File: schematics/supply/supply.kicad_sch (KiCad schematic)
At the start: 4 parts, among them J1 Conn_01x02_Pin, J2 Conn_01x02_Pin, J3 Conn_01x01_Pin, J4 Conn_01x01_Pin

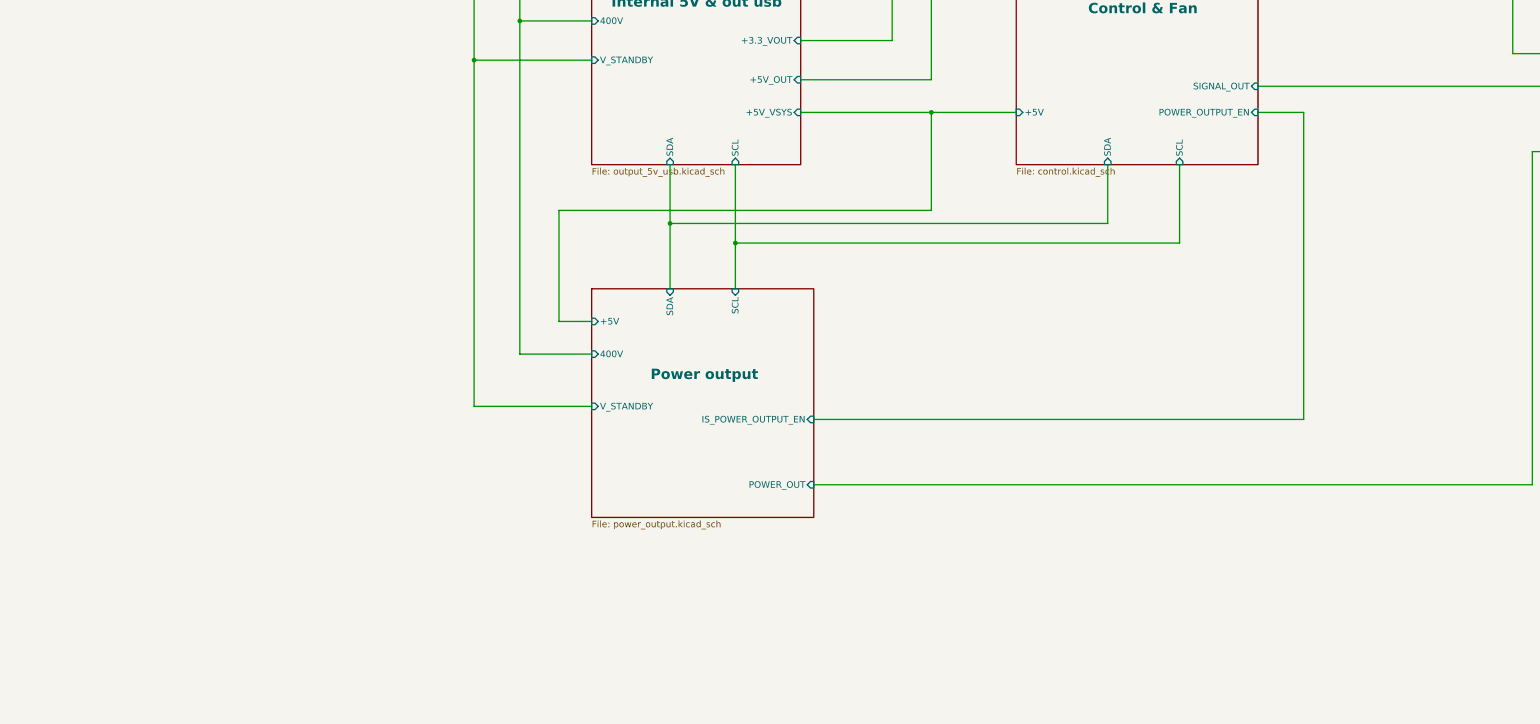
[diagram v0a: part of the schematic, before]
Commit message: Prepare to move USB ports to a few millimenters outside
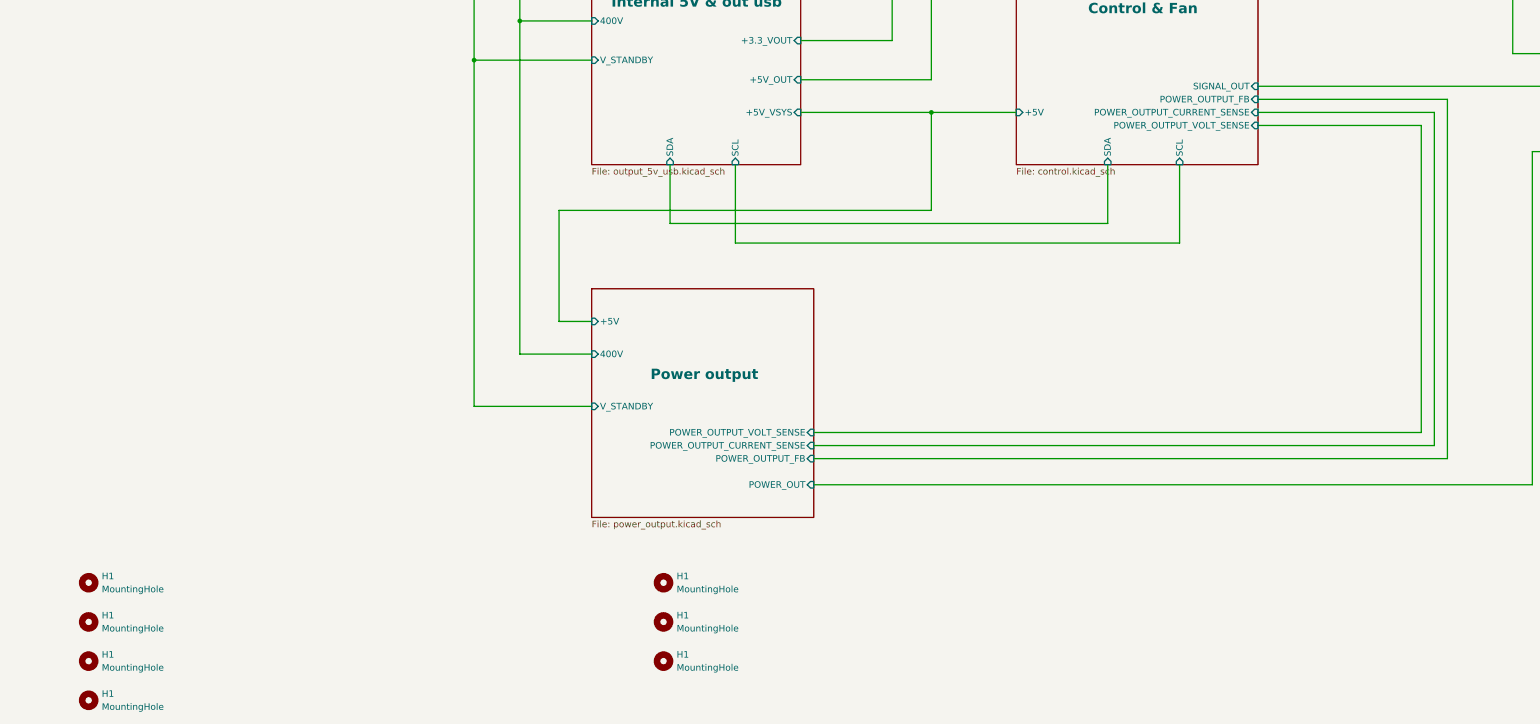
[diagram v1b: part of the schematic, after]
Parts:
- added H1 (x7): MountingHole, MountingHole:MountingHole_2.2mm_M2, symbol Mechanical:MountingHole
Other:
- sheet Control & Fan ports: added POWER_OUTPUT_CURRENT_SENSE, POWER_OUTPUT_FB, POWER_OUTPUT_VOLT_SENSE; removed POWER_OUTPUT_EN
- sheet Power output ports: added POWER_OUTPUT_CURRENT_SENSE, POWER_OUTPUT_FB, POWER_OUTPUT_VOLT_SENSE; removed IS_POWER_OUTPUT_EN, SCL, SDA

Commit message: Updated boards
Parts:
- added H1 (x2): MountingHole, MountingHole:MountingHole_2.2mm_M2, symbol Mechanical:MountingHole
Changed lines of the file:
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@@
+    )
+  )
+  (symbol (lib_id "Mechanical:MountingHole") (at 31.75 269.24 0) (unit 1)
+    (in_bom yes) (on_board yes) (dnp no) (fields_autoplaced)
+    (property "Reference" "H1" (at 34.29 267.9699 0)
+      (effects (font (size 1.27 1.27)) (justify left))
+    )
+    (property "Value" "MountingHole" (at 34.29 270.5099 0)
+      (effects (font (size 1.27 1.27)) (justify left))
+    )
+    (property "Footprint" "MountingHole:MountingHole_2.2mm_M2" (at 31.75 269.24 0)
+      (effects (font (size 1.27 1.27)) hide)
+    )
+    (property "Datasheet" "~" (at 31.75 269.24 0)
+      (effects (font (size 1.27 1.27)) hide)
+    )
+    (instances
+      (project "xray"
+        (path "/002cc585-3681-421a-8dca-b0910197d82b"
+          (reference "H1") (unit 1)
+        )
+      )
+      (project "supply"
+        (path "/1e139717-fcd1-4008-a6ea-4c993845e928"
+          (reference "H5") (unit 1)
+        )
+      )
+    )
+  )
+  (symbol (lib_id "Mechanical:MountingHole") (at 31.75 276.86 0) (unit 1)
+    (in_bom yes) (on_board yes) (dnp no) (fields_autoplaced)
+    (property "Reference" "H1" (at 34.29 275.5899 0)
+      (effects (font (size 1.27 1.27)) (justify left))
+    )
+    (property "Value" "MountingHole" (at 34.29 278.1299 0)
+      (effects (font (size 1.27 1.27)) (justify left))
+    )
+    (property "Footprint" "MountingHole:MountingHole_2.2mm_M2" (at 31.75 276.86 0)
+      (effects (font (size 1.27 1.27)) hide)
+    )
+    (property "Datasheet" "~" (at 31.75 276.86 0)
+      (effects (font (size 1.27 1.27)) hide)
+    )
+    (instances
+      (project "xray"
+        (path "/002cc585-3681-421a-8dca-b0910197d82b"
+          (reference "H1") (unit 1)
+        )
+      )
+      (project "supply"
+        (path "/1e139717-fcd1-4008-a6ea-4c993845e928"
+          (reference "H6") (unit 1)
+        )
+      )
     )
   )
@@
       (project "supply"
         (path "/1e139717-fcd1-4008-a6ea-4c993845e928"
-          (reference "H5") (unit 1)
+          (reference "H7") (unit 1)
         )
       )
@@
       (project "supply"
         (path "/1e139717-fcd1-4008-a6ea-4c993845e928"
-          (reference "H7") (unit 1)
+          (reference "H9") (unit 1)
         )
       )
@@
       (project "supply"
         (path "/1e139717-fcd1-4008-a6ea-4c993845e928"
-          (reference "H6") (unit 1)
-        )
-      )
+          (reference "H8") (unit 1)
+        )
+      )

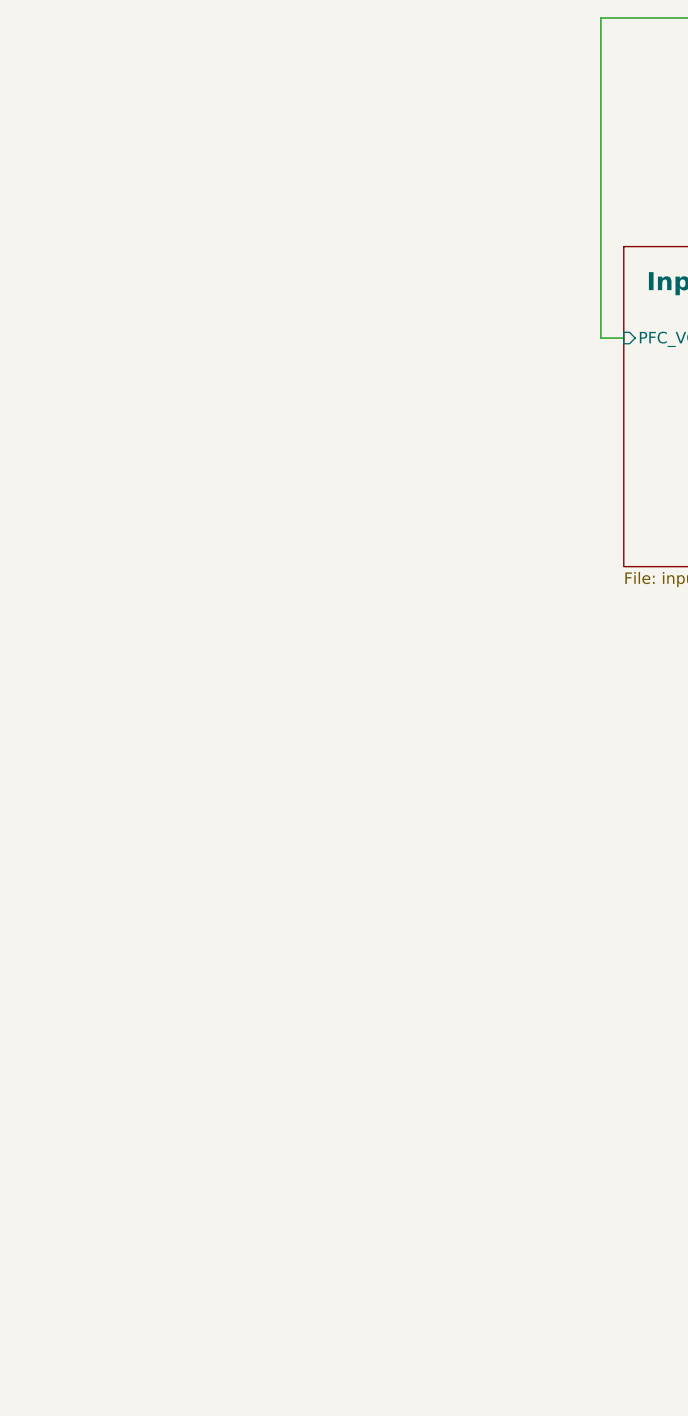
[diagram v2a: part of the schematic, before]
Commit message: prepare to add current measurement for a middle-current 5V and 3.3V lines
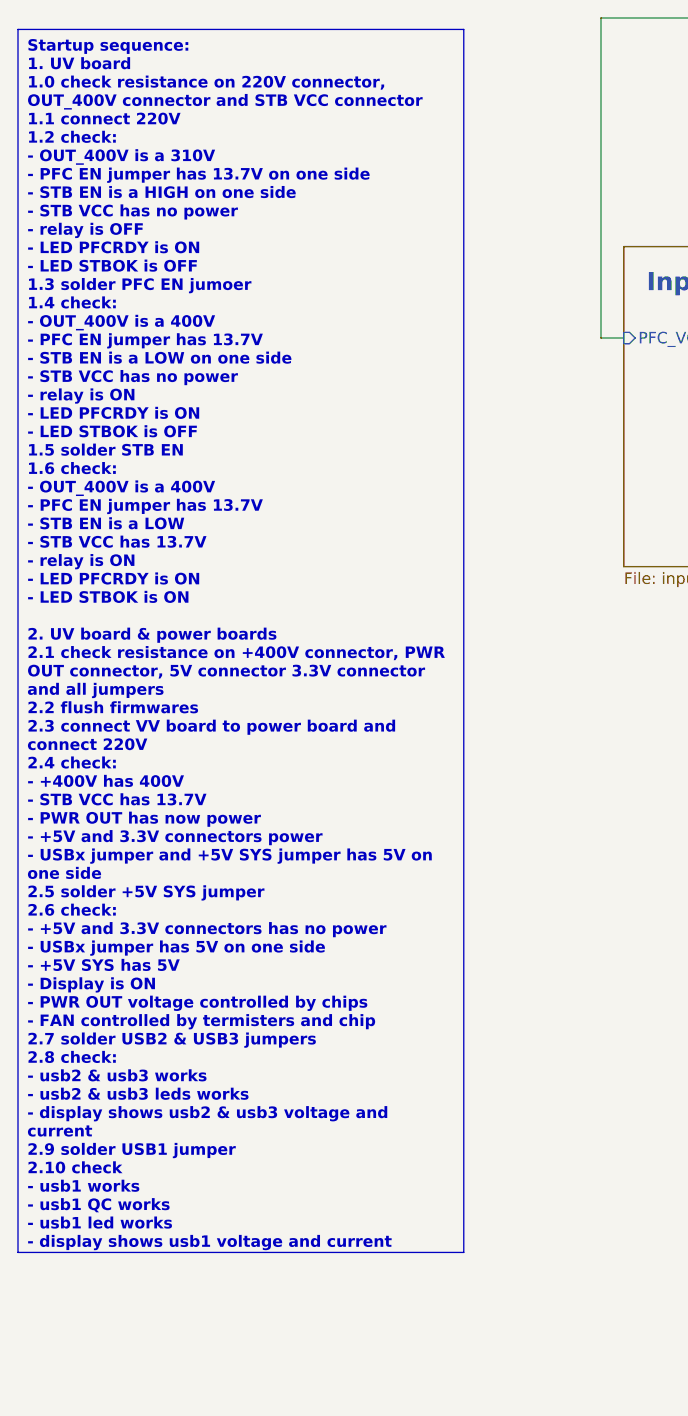
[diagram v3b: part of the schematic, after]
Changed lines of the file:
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@@
     (stroke (width 0) (type default))
+  )
+  (text_box "Startup sequence:\n1. UV board\n1.0 check resistance on 220V connector, OUT_400V connector and STB VCC connector\n1.1 connect 220V\n1.2 check: \n    - OUT_400V is a 310V\n    - PFC EN jumper has 13.7V on one side \n    - STB EN is a HIGH on one side\n    - STB VCC has no power\n    - relay is OFF\n    - LED PFCRDY is ON\n    - LED STBOK is OFF\n1.3 solder PFC EN jumoer\n1.4 check:\n    - OUT_400V is a 400V\n    - PFC EN jumper has 13.7V\n    - STB EN is a LOW on one side\n    - STB VCC has no power\n    - relay is ON\n    - LED PFCRDY is ON\n    - LED STBOK is OFF\n1.5 solder STB EN\n1.6 check:\n    - OUT_400V is a 400V\n    - PFC EN jumper has 13.7V\n    - STB EN is a LOW\n    - STB VCC has 13.7V\n    - relay is ON\n    - LED PFCRDY is ON\n    - LED STBOK is ON\n\n2. UV board & power boards\n2.1 check resistance on +400V connector, PWR OUT connector, 5V connector 3.3V connector and all jumpers\n2.2 flush firmwares\n2.3 connect VV board to power board and connect 220V\n2.4 check:\n    - +400V has 400V\n    - STB VCC has 13.7V\n    - PWR OUT has now power\n    - +5V and 3.3V connectors power\n    - USBx jumper and +5V SYS jumper has 5V on one side\n2.5 solder +5V SYS jumper\n2.6 check:\n    - +5V and 3.3V connectors has no power\n    - USBx jumper has 5V on one side\n    - +5V SYS has 5V\n    - Display is ON\n    - PWR OUT voltage controlled by chips\n    - FAN controlled by termisters and chip\n2.7 solder USB2 & USB3 jumpers\n2.8 check: \n    - usb2 & usb3 works\n    - usb2 & usb3 leds works\n    - display shows usb2 & usb3 voltage and current\n2.9 solder USB1 jumper\n2.10 check \n    - usb1 works\n    - usb1 QC works\n    - usb1 led works\n    - display shows usb1 voltage and current\n"
+    (at -48.26 30.48 0) (size 49.53 135.89)
+    (stroke (width 0) (type default))
+    (fill (type none))
+    (effects (font (size 1.27 1.27) (thickness 0.254) bold) (justify left top))
   )
   (symbol (lib_id "Mechanical:MountingHole") (at 31.75 254 0) (unit 1)

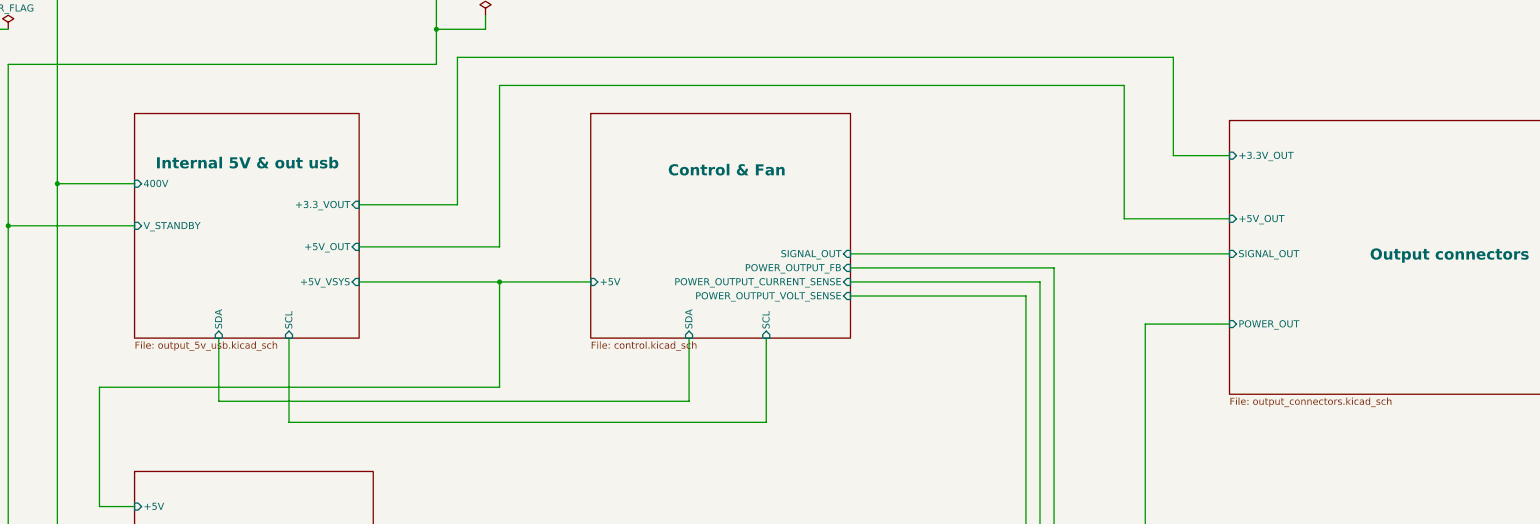
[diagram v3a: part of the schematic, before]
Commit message: prepare to replace inductor on 5V power line
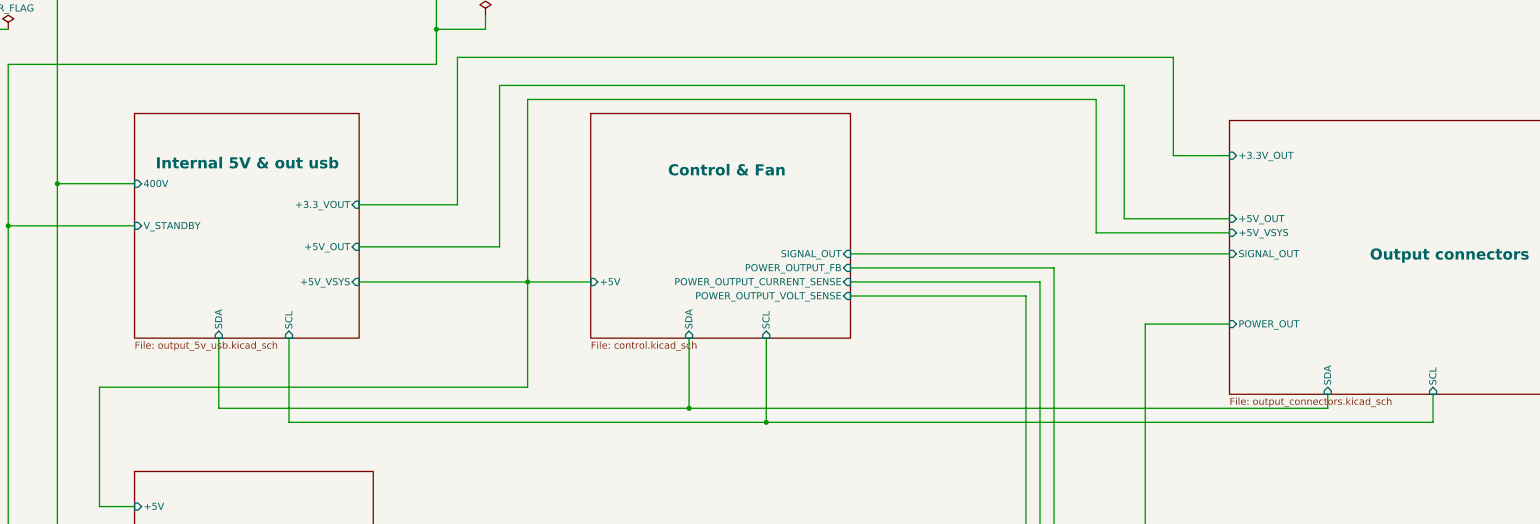
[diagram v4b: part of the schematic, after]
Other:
- sheet Output connectors ports: added +5V_VSYS, SCL, SDA; removed none
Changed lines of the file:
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@@
   (junction (at 184.15 101.6) (diameter 0) (color 0 0 0 0)
   )
-  (junction (at 195.58 147.32) (diameter 0) (color 0 0 0 0)
-  )
   (junction (at 97.79 101.6) (diameter 0) (color 0 0 0 0)
   )
   (junction (at 71.12 73.66) (diameter 0) (color 0 0 0 0)
   )
+  (junction (at 243.84 172.72) (diameter 0) (color 0 0 0 0)
+  )
+  (junction (at 200.66 147.32) (diameter 0) (color 0 0 0 0)
+  )
   (junction (at 106.68 137.16) (diameter 0) (color 0 0 0 0)
   )
+  (junction (at 229.87 170.18) (diameter 0) (color 0 0 0 0)
+  )
   (wire (pts (xy 129.54 204.47) (xy 106.68 204.47))
     (stroke (width 0) (type default))
@@
     (stroke (width 0) (type default))
   )
-  (wire (pts (xy 195.58 147.32) (xy 212.09 147.32))
+  (wire (pts (xy 170.18 147.32) (xy 200.66 147.32))
     (stroke (width 0) (type default))
   )
@@
     (stroke (width 0) (type default))
   )
+  (wire (pts (xy 364.49 167.64) (xy 364.49 172.72))
+    (stroke (width 0) (type default))
+  )
   (wire (pts (xy 115.57 194.31) (xy 115.57 129.54))
     (stroke (width 0) (type default))
@@
     (stroke (width 0) (type default))
   )
+  (wire (pts (xy 303.53 114.3) (xy 200.66 114.3))
+    (stroke (width 0) (type default))
+  )
   (wire (pts (xy 184.15 90.17) (xy 184.15 101.6))
     (stroke (width 0) (type default))
@@
     (stroke (width 0) (type default))
   )
+  (wire (pts (xy 200.66 147.32) (xy 212.09 147.32))
+    (stroke (width 0) (type default))
+  )
   (wire (pts (xy 317.5 106.68) (xy 317.5 124.46))
     (stroke (width 0) (type default))
@@
     (stroke (width 0) (type default))
   )
-  (wire (pts (xy 170.18 147.32) (xy 195.58 147.32))
-    (stroke (width 0) (type default))
-  )
   (wire (pts (xy 184.15 107.95) (xy 106.68 107.95))
     (stroke (width 0) (type default))
@@
     (stroke (width 0) (type default))
   )
+  (wire (pts (xy 345.44 170.18) (xy 229.87 170.18))
+    (stroke (width 0) (type default))
+  )
   (wire (pts (xy 195.58 140.97) (xy 170.18 140.97))
     (stroke (width 0) (type default))
@@
     (stroke (width 0) (type default))
   )
-  (wire (pts (xy 195.58 147.32) (xy 195.58 166.37))
+  (wire (pts (xy 200.66 147.32) (xy 200.66 166.37))
+    (stroke (width 0) (type default))
+  )
+  (wire (pts (xy 327.66 138.43) (xy 303.53 138.43))
     (stroke (width 0) (type default))
   )
@@
     (stroke (width 0) (type default))
   )
+  (wire (pts (xy 345.44 167.64) (xy 345.44 170.18))
+    (stroke (width 0) (type default))
+  )
   (wire (pts (xy 243.84 172.72) (xy 157.48 172.72))
     (stroke (width 0) (type default))
   )
+  (wire (pts (xy 364.49 172.72) (xy 243.84 172.72))
+    (stroke (width 0) (type default))
+  )
   (wire (pts (xy 115.57 129.54) (xy 115.57 95.25))
     (stroke (width 0) (type default))
@@
     (stroke (width 0) (type default))
   )
-  (wire (pts (xy 123.19 166.37) (xy 195.58 166.37))
-    (stroke (width 0) (type default))
-  )
-  (wire (pts (xy 229.87 168.91) (xy 144.78 168.91))
+  (wire (pts (xy 123.19 166.37) (xy 200.66 166.37))
+    (stroke (width 0) (type default))
+  )
+  (wire (pts (xy 229.87 170.18) (xy 144.78 170.18))
+    (stroke (width 0) (type default))
+  )
+  (wire (pts (xy 303.53 138.43) (xy 303.53 114.3))
     (stroke (width 0) (type default))
   )
@@
     (stroke (width 0) (type default))
   )
+  (wire (pts (xy 200.66 114.3) (xy 200.66 147.32))
+    (stroke (width 0) (type default))
+  )
   (wire (pts (xy 60.96 105.41) (xy 71.12 105.41))
     (stroke (width 0) (type default))
@@
     (stroke (width 0) (type default))
   )
-  (wire (pts (xy 144.78 157.48) (xy 144.78 168.91))
+  (wire (pts (xy 144.78 157.48) (xy 144.78 170.18))
     (stroke (width 0) (type default))
   )
@@
     (stroke (width 0) (type default))
   )
-  (wire (pts (xy 229.87 157.48) (xy 229.87 168.91))
+  (wire (pts (xy 229.87 157.48) (xy 229.87 170.18))
     (stroke (width 0) (type default))
   )
@@
       (effects (font (size 1.27 1.27)) (justify left))
     )
+    (pin "SDA" input (at 345.44 167.64 270)
+      (effects (font (size 1.27 1.27)) (justify left))
+    )
+    (pin "SCL" input (at 364.49 167.64 270)
+      (effects (font (size 1.27 1.27)) (justify left))
+    )
+    (pin "+5V_VSYS" input (at 327.66 138.43 180)
+      (effects (font (size 1.27 1.27)) (justify left))
+    )
